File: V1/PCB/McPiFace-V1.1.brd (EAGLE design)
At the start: 44 x 88 mm, 10 parts, among them J1 MC_PI_FACE_CONNECTORS_LEDSSIDE

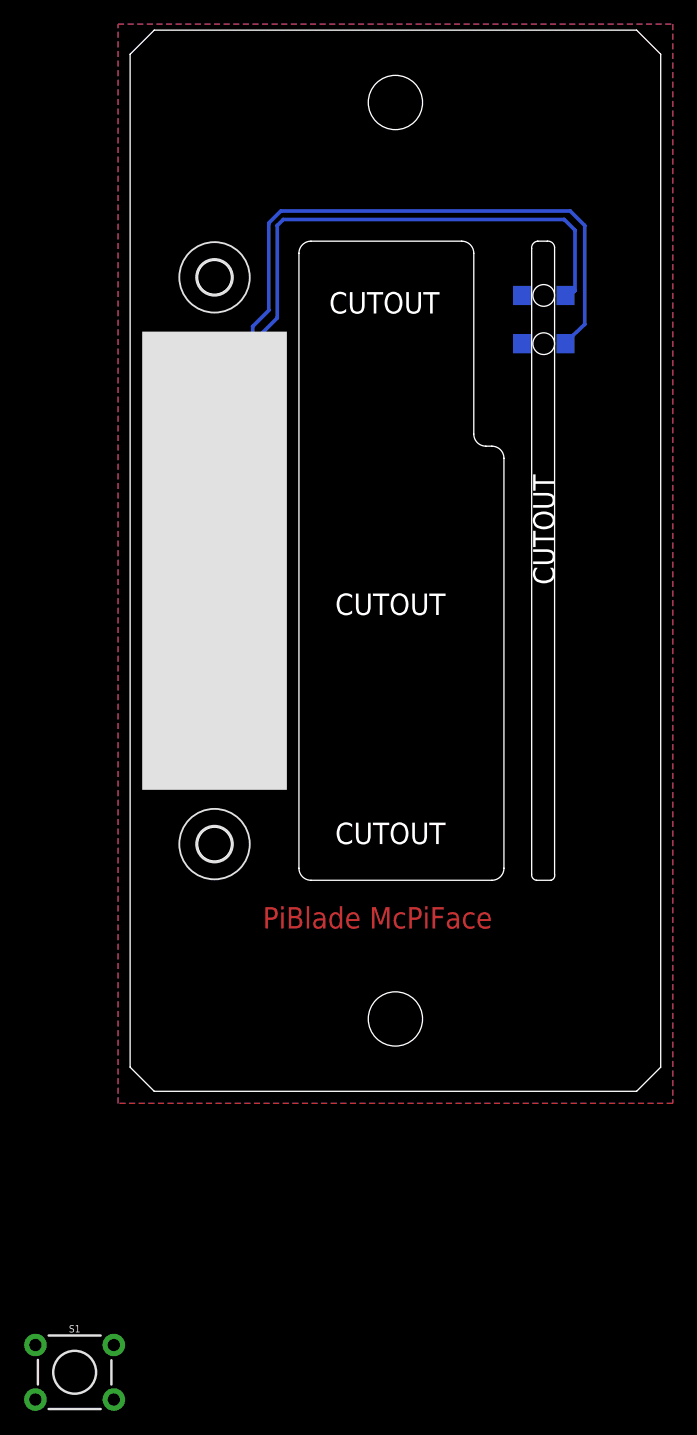
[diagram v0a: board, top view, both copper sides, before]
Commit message: Adding V1.1 PCB.
Uses common layout for LEDs, removed vent hole.
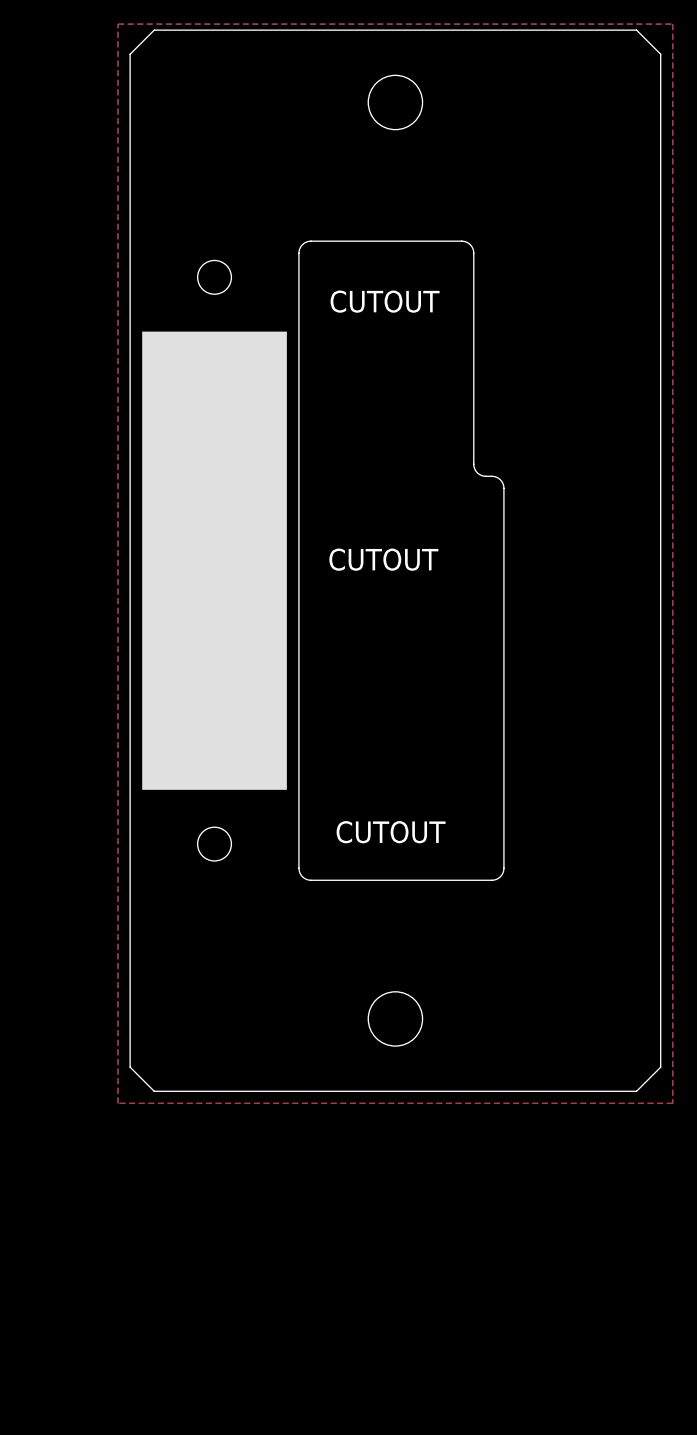
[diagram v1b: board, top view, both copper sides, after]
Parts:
- removed H3, H4: MOUNT-HOLE2.8, holes:2,8
- added U$1: MC_PI_FACE_PANELSINGLE, McPiFace:MC_PI_FACE_JOINT
- D2: value (none) -> Green
- D3: value (none) -> Red
- R1, R2: device SparkFun-Resistors:1206 -> SparkFun-Resistors:0805
- moved S1 53.6 mm to (7.00, 29.0)
- moved D2 30.4 mm to (4.00, 59.0), turned to 90 degrees
- moved D3 25.3 mm to (10.0, 59.0), turned to 90 degrees
- moved FRAME1 22.0 mm to (-3.80, -11.6)
- moved J1 8.84 mm to (6.80, 49.8)
- moved R1 6.62 mm to (10.0, 53.4), turned to 90 degrees
- moved R2 3.84 mm to (4.00, 53.4), turned to 90 degrees
- moved LOGO1 1.10 mm to (35.6, 5.90), turned to 0 degrees
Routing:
- net N$3: track 60.7 -> 2.90 mm
- net N$4: track 58.3 -> 2.90 mm
- net N$6: track 13.2 -> 4.77 mm
- net N$7: track 15.9 -> 20.6 mm
- net N$5: track 6.96 -> 5.17 mm
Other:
- outline, holes or cut-outs redrawn
- board text added: "McPiFace.com"
- board text added: "Stephen Harrison"
- board text added: "V1.1"
- board text added: "http://github.com/McPiFace/McPiFace"
- board text removed: "CUTOUT"
- board text removed: "PiBlade McPiFace"
- board text removed: "http://github.com/ThingySticks/PiBlade"
